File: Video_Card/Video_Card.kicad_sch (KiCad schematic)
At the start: 0 parts

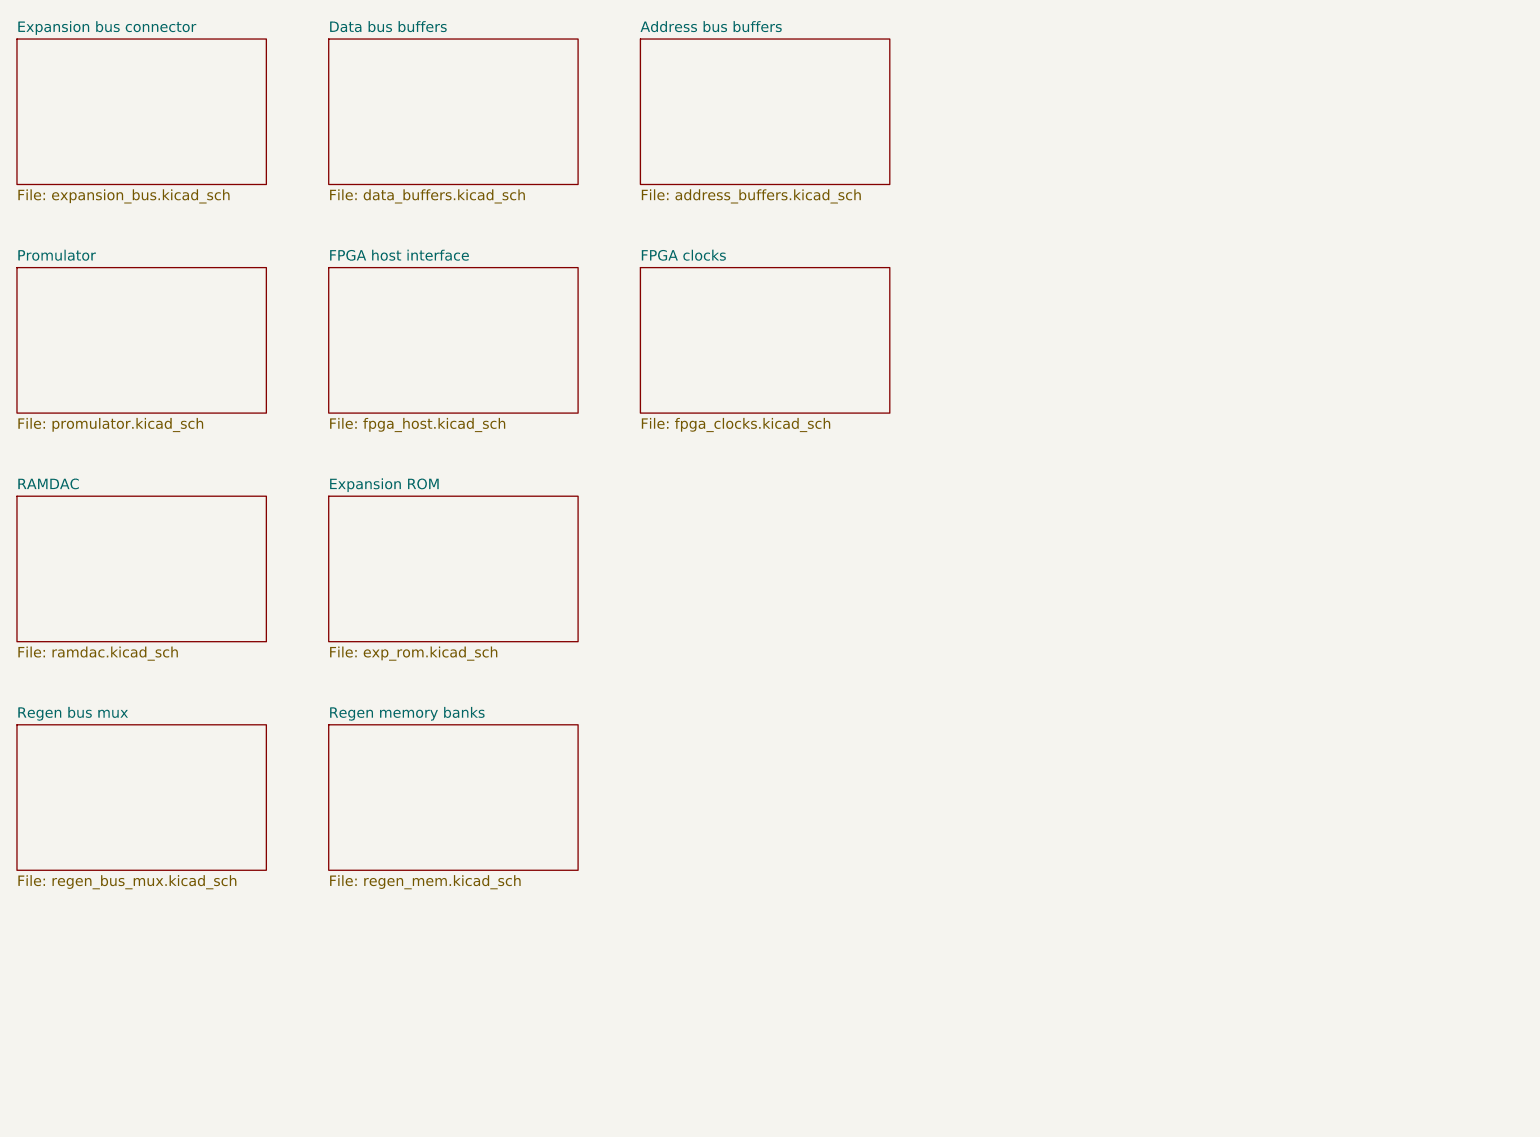
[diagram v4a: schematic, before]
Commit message: Work to date
So much to list ....

* Changed expansion ROM to 16 bit wide to remove some components
* Tried moving peripherals over to an 8 bit dedicated bus, but will have to revert this to reduce component count
* Fleshed out keyboard and I2C controller circuits
* Tried to fit in a font RAM, but I am 50/50 whether this will stick

And a lot more I am sure.
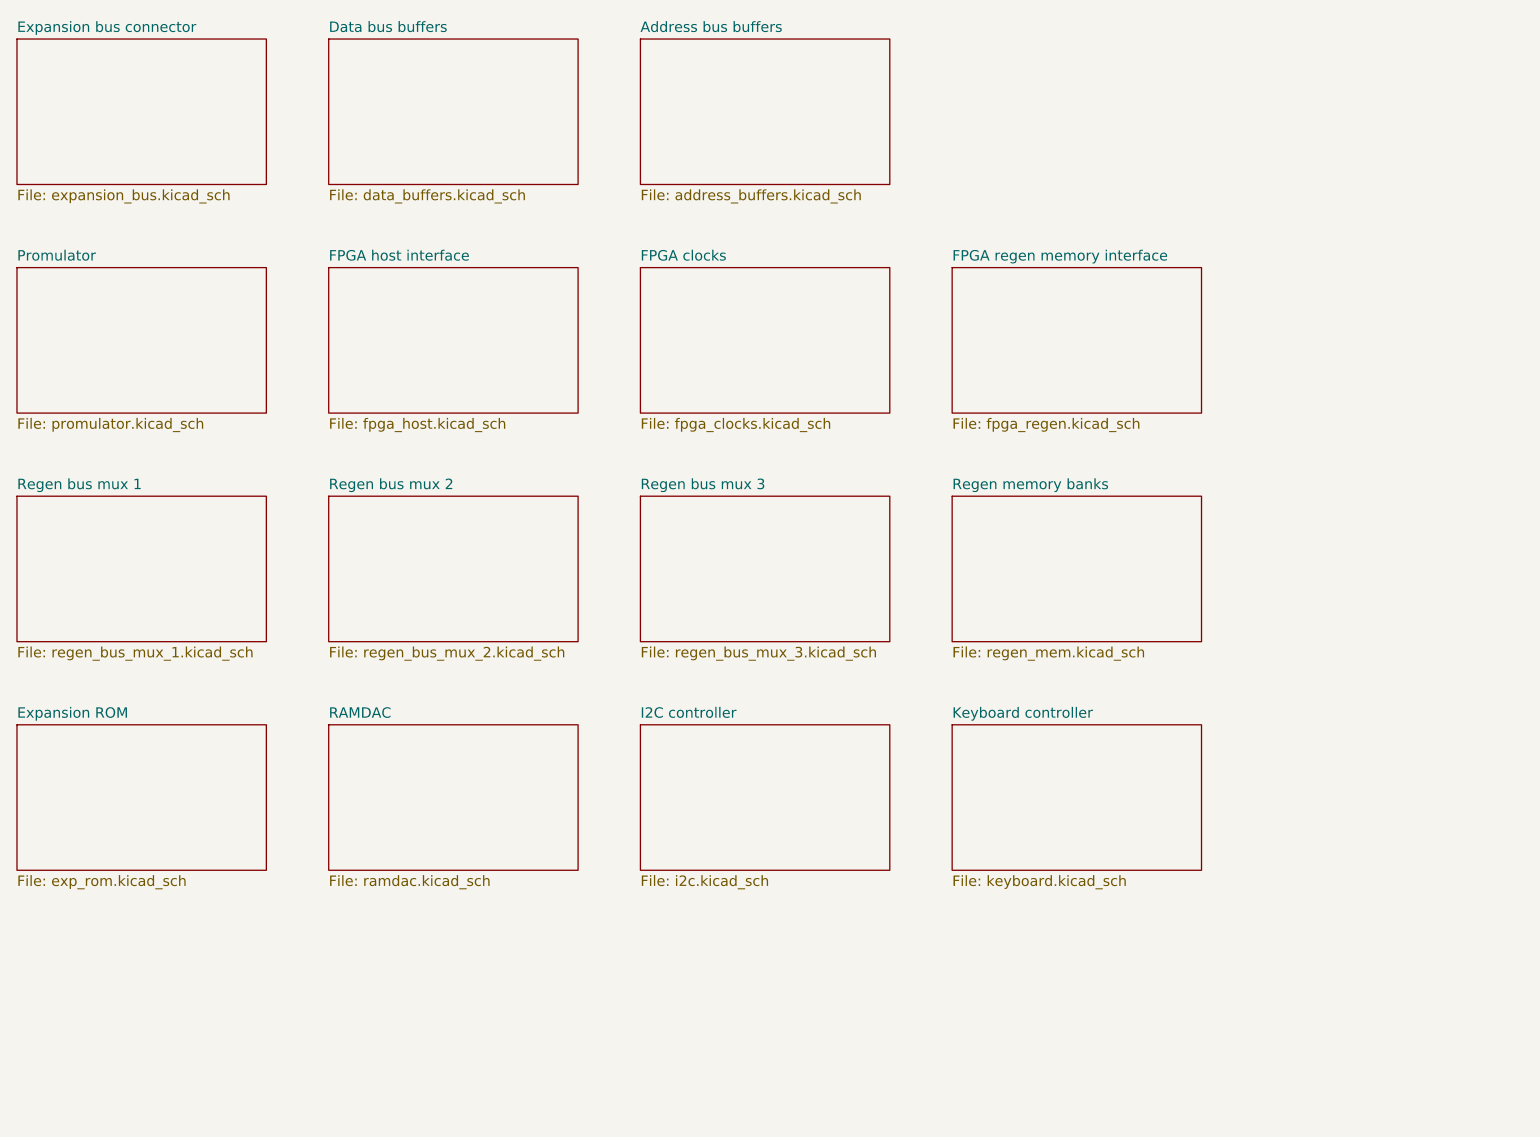
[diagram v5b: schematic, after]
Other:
- removed sheet Regen bus mux
- added sheet FPGA regen memory interface (fpga_regen.kicad_sch)
- added sheet I2C controller (i2c.kicad_sch)
- added sheet Keyboard controller (keyboard.kicad_sch)
- added sheet Regen bus mux 1 (regen_bus_mux_1.kicad_sch)
- added sheet Regen bus mux 2 (regen_bus_mux_2.kicad_sch)
- added sheet Regen bus mux 3 (regen_bus_mux_3.kicad_sch)
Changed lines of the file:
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@@
+	)
+	(sheet
+		(at 142.24 109.22)
+		(size 30.48 17.78)
+		(fields_autoplaced yes)
+		(stroke
+			(width 0.1524)
+			(type solid)
+		)
+		(fill
+			(color 0 0 0 0.0000)
+		)
+		(property "Sheetname" "Keyboard controller"
+			(at 142.24 108.5084 0)
+			(effects
+				(font
+					(size 1.27 1.27)
+				)
+				(justify left bottom)
+			)
+		)
+		(property "Sheetfile" "keyboard.kicad_sch"
+			(at 142.24 127.5846 0)
+			(effects
+				(font
+					(size 1.27 1.27)
+				)
+				(justify left top)
+			)
+		)
+		(instances
+			(project "Video_Card"
+				(path "/ae665dca-cabf-48ec-b560-2bab32dde7c4"
+					(page "17")
+				)
+			)
+		)
+	)
+	(sheet
+		(at 66.04 81.28)
+		(size 30.48 17.78)
+		(fields_autoplaced yes)
+		(stroke
+			(width 0.1524)
+			(type solid)
+		)
+		(fill
+			(color 0 0 0 0.0000)
+		)
+		(property "Sheetname" "Regen bus mux 2"
+			(at 66.04 80.5684 0)
+			(effects
+				(font
+					(size 1.27 1.27)
+				)
+				(justify left bottom)
+			)
+		)
+		(property "Sheetfile" "regen_bus_mux_2.kicad_sch"
+			(at 66.04 99.6446 0)
+			(effects
+				(font
+					(size 1.27 1.27)
+				)
+				(justify left top)
+			)
+		)
+		(instances
+			(project "Video_Card"
+				(path "/ae665dca-cabf-48ec-b560-2bab32dde7c4"
+					(page "10")
+				)
+			)
+		)
 	)
 	(sheet
@@
 	)
 	(sheet
+		(at 142.24 81.28)
+		(size 30.48 17.78)
+		(fields_autoplaced yes)
+		(stroke
+			(width 0.1524)
+			(type solid)
+		)
+		(fill
+			(color 0 0 0 0.0000)
+		)
+		(property "Sheetname" "Regen memory banks"
+			(at 142.24 80.5684 0)
+			(effects
+				(font
+					(size 1.27 1.27)
+				)
+				(justify left bottom)
+			)
+		)
+		(property "Sheetfile" "regen_mem.kicad_sch"
+			(at 142.24 99.6446 0)
+			(effects
+				(font
+					(size 1.27 1.27)
+				)
+				(justify left top)
+			)
+		)
+		(instances
+			(project "Video_Card"
+				(path "/ae665dca-cabf-48ec-b560-2bab32dde7c4"
+					(page "12")
+				)
+			)
+		)
+	)
+	(sheet
 		(at 66.04 109.22)
 		(size 30.48 17.78)
@@
 			(color 0 0 0 0.0000)
 		)
-		(property "Sheetname" "Regen memory banks"
+		(property "Sheetname" "RAMDAC"
 			(at 66.04 108.5084 0)
 			(effects
@@
 			)
 		)
-		(property "Sheetfile" "regen_mem.kicad_sch"
+		(property "Sheetfile" "ramdac.kicad_sch"
 			(at 66.04 127.5846 0)
 			(effects
@@
 			(project "Video_Card"
 				(path "/ae665dca-cabf-48ec-b560-2bab32dde7c4"
-					(page "11")
-				)
-			)
-		)
-	)
-	(sheet
-		(at 27.94 81.28)
-		(size 30.48 17.78)
-		(fields_autoplaced yes)
-		(stroke
-			(width 0.1524)
-			(type solid)
-		)
-		(fill
-			(color 0 0 0 0.0000)
-		)
-		(property "Sheetname" "RAMDAC"
-			(at 27.94 80.5684 0)
-			(effects
-				(font
-					(size 1.27 1.27)
-				)
-				(justify left bottom)
-			)
-		)
-		(property "Sheetfile" "ramdac.kicad_sch"
-			(at 27.94 99.6446 0)
-			(effects
-				(font
-					(size 1.27 1.27)
-				)
-				(justify left top)
-			)
-		)
-		(instances
-			(project "Video_Card"
-				(path "/ae665dca-cabf-48ec-b560-2bab32dde7c4"
-					(page "8")
+					(page "15")
 				)
 			)
@@
 	)
 	(sheet
-		(at 66.04 81.28)
+		(at 27.94 109.22)
 		(size 30.48 17.78)
 		(fields_autoplaced yes)
@@
 		)
 		(property "Sheetname" "Expansion ROM"
-			(at 66.04 80.5684 0)
+			(at 27.94 108.5084 0)
 			(effects
 				(font
@@
 		)
 		(property "Sheetfile" "exp_rom.kicad_sch"
-			(at 66.04 99.6446 0)
-			(effects
-				(font
-					(size 1.27 1.27)
-				)
-				(justify left top)
-			)
-		)
-		(instances
-			(project "Video_Card"
-				(path "/ae665dca-cabf-48ec-b560-2bab32dde7c4"
-					(page "9")
+			(at 27.94 127.5846 0)
+			(effects
+				(font
+					(size 1.27 1.27)
+				)
+				(justify left top)
+			)
+		)
+		(instances
+			(project "Video_Card"
+				(path "/ae665dca-cabf-48ec-b560-2bab32dde7c4"
+					(page "14")
 				)
 			)
@@
 	)
 	(sheet
-		(at 27.94 109.22)
-		(size 30.48 17.78)
-		(fields_autoplaced yes)
-		(stroke
-			(width 0.1524)
-			(type solid)
-		)
-		(fill
-			(color 0 0 0 0.0000)
-		)
-		(property "Sheetname" "Regen bus mux"
-			(at 27.94 108.5084 0)
-			(effects
-				(font
-					(size 1.27 1.27)
-				)
-				(justify left bottom)
-			)
-		)
-		(property "Sheetfile" "regen_bus_mux.kicad_sch"
-			(at 27.94 127.5846 0)
-			(effects
-				(font
-					(size 1.27 1.27)
-				)
-				(justify left top)
-			)
-		)
-		(instances
-			(project "Video_Card"
-				(path "/ae665dca-cabf-48ec-b560-2bab32dde7c4"
-					(page "10")
-				)
-			)
+		(at 27.94 81.28)
+		(size 30.48 17.78)
+		(fields_autoplaced yes)
+		(stroke
+			(width 0.1524)
+			(type solid)
+		)
+		(fill
+			(color 0 0 0 0.0000)
+		)
+		(property "Sheetname" "Regen bus mux 1"
+			(at 27.94 80.5684 0)
+			(effects
+				(font
+					(size 1.27 1.27)
+				)
+				(justify left bottom)
+			)
+		)
+		(property "Sheetfile" "regen_bus_mux_1.kicad_sch"
+			(at 27.94 99.6446 0)
+			(effects
+				(font
+					(size 1.27 1.27)
+				)
+				(justify left top)
+			)
+		)
+		(instances
+			(project "Video_Card"
+				(path "/ae665dca-cabf-48ec-b560-2bab32dde7c4"
+					(page "9")
+				)
+			)
+		)
+	)
+	(sheet
+		(at 104.14 81.28)
+		(size 30.48 17.78)
+		(fields_autoplaced yes)
+		(stroke
+			(width 0.1524)
+			(type solid)
+		)
+		(fill
+			(color 0 0 0 0.0000)
+		)
+		(property "Sheetname" "Regen bus mux 3"
+			(at 104.14 80.5684 0)
+			(effects
+				(font
+					(size 1.27 1.27)
+				)
+				(justify left bottom)
+			)
+		)
+		(property "Sheetfile" "regen_bus_mux_3.kicad_sch"
+			(at 104.14 99.6446 0)
+			(effects
+				(font
+					(size 1.27 1.27)
+				)
+				(justify left top)
+			)
+		)
+		(instances
+			(project "Video_Card"
+				(path "/ae665dca-cabf-48ec-b560-2bab32dde7c4"
+					(page "11")
+				)
+			)
+		)
+	)
+	(sheet
+		(at 142.24 53.34)
+		(size 30.48 17.78)
+		(fields_autoplaced yes)
+		(stroke
+			(width 0.1524)
+			(type solid)
+		)
+		(fill
+			(color 0 0 0 0.0000)
+		)
+		(property "Sheetname" "FPGA regen memory interface"
+			(at 142.24 52.6284 0)
+			(effects
+				(font
+					(size 1.27 1.27)
+				)
+				(justify left bottom)
+			)
+		)
+		(property "Sheetfile" "fpga_regen.kicad_sch"
+			(at 142.24 71.7046 0)
+			(effects
+				(font
+					(size 1.27 1.27)
+				)
+				(justify left top)
+			)
+		)
+		(instances
+			(project "Video_Card"
+				(path "/ae665dca-cabf-48ec-b560-2bab32dde7c4"
+					(page "8")
+				)
+			)
+		)
+	)
+	(sheet
+		(at 104.14 109.22)
+		(size 30.48 17.78)
+		(fields_autoplaced yes)
+		(stroke
+			(width 0.1524)
+			(type solid)
+		)
+		(fill
+			(color 0 0 0 0.0000)
+		)
+		(property "Sheetname" "I2C controller"
+			(at 104.14 108.5084 0)
+			(effects
+				(font
+					(size 1.27 1.27)
+				)
+				(justify left bottom)
+			)
+		)
+		(property "Sheetfile" "i2c.kicad_sch"
+			(at 104.14 127.5846 0)
+			(effects
+				(font
+					(size 1.27 1.27)
+				)
+				(justify left top)
+			)
+		)
+		(instances
+			(project "Video_Card"
+				(path "/ae665dca-cabf-48ec-b560-2bab32dde7c4"
+					(page "16")
+				)
+			)

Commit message: Final work for rev 1
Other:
- removed sheet FPGA clocks
- added sheet Font RAM (font_ram_2.kicad_sch)
- added sheet Mechanical (mechanical.kicad_sch)
- added sheet Power (power.kicad_sch)
- title: VGA COMPATIBLE VIDEO CARD -> VGA VIDEO, AND PS/2 KEYBOARD AND MOUSE CARD
